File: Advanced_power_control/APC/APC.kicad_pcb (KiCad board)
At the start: 4 copper layers, 60.2 x 84.5 mm, 51 parts, among them J1 AVR-JTAG-10, J10 CMD_IN, J11 PWR_V_SEL, J12 12/24 V_IN, J13 220 OUT, J2 EM_STOP_INT, J3 STATUS_LED, J4 EM_STOP, J5 PWR_BTN, J6 POWER_LED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

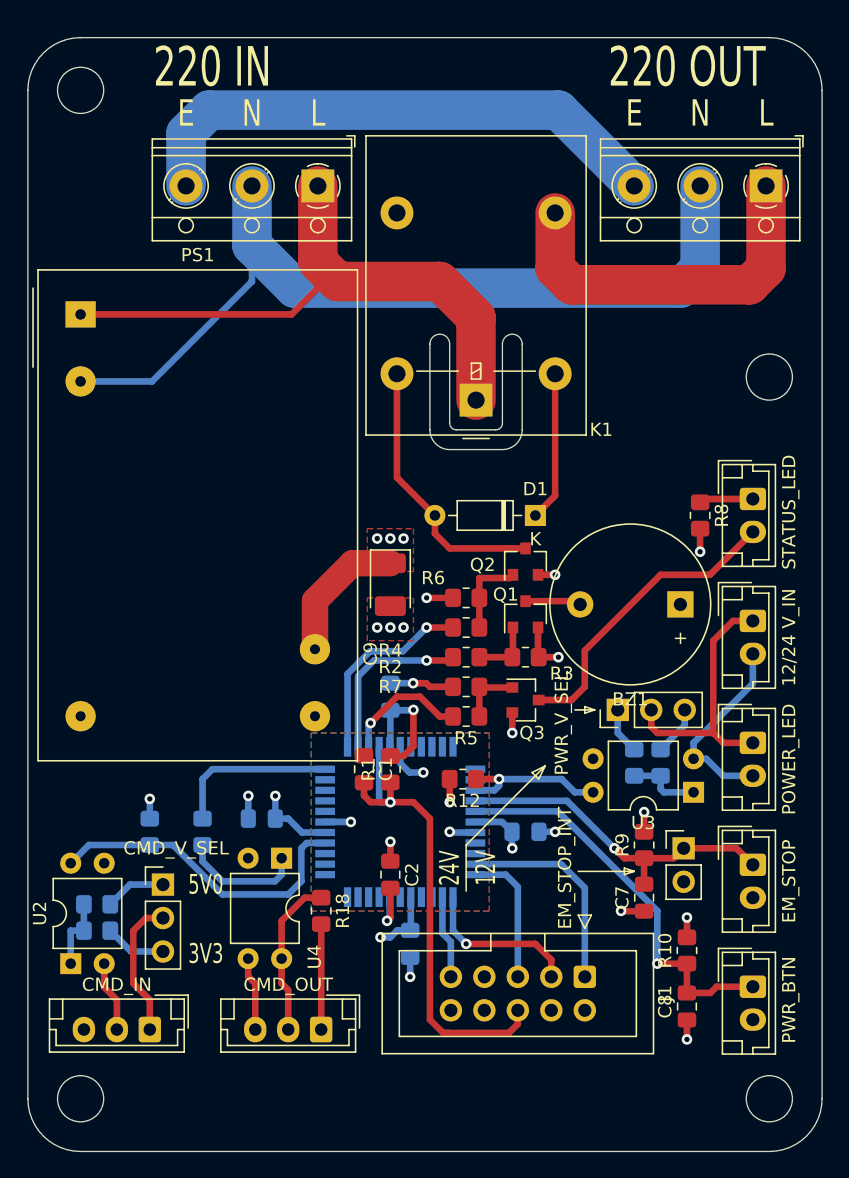
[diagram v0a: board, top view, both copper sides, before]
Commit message: minimize pcb size
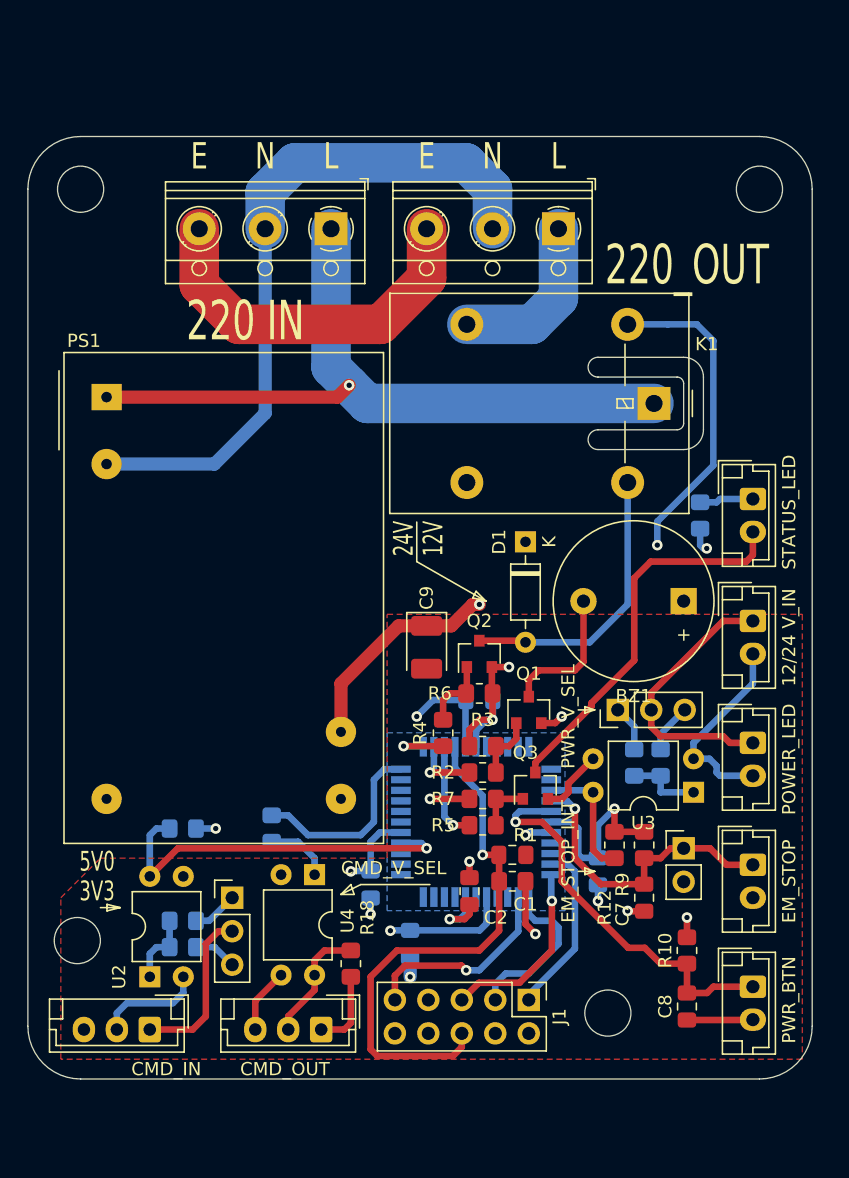
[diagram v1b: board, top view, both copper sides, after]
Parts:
- J1: footprint Connector_IDC:IDC-Header_2x05_P2.54mm_Vertical -> Connector_PinHeader_2.54mm:PinHeader_2x05_P2.54mm_Vertical
- J13: value 220 OUT -> 220_OUT
- R8: moved to B.Cu
- moved J13 16.1 mm to (126.5, 37.0)
- moved K1 13.5 mm to (133.8, 50.2), turned to 270 degrees
- moved C1 13.0 mm to (123.0, 84.5), turned to 180 degrees
- moved R1 12.6 mm to (123.0, 86.5), turned to 0 degrees
- moved R12 12.5 mm to (130.8, 83.8), turned to 90 degrees
- moved C5 9.65 mm to (112.2, 86.8), turned to 90 degrees
- moved R2 8.84 mm to (120.8, 78.2)
- moved R7 8.59 mm to (120.8, 80.2)
- moved R5 8.34 mm to (120.8, 82.2)
- moved R4 8.19 mm to (117.8, 75.2), turned to 270 degrees
- moved Q2 7.83 mm to (120.5, 69.2)
- moved R3 7.49 mm to (120.8, 76.2), turned to 0 degrees
- moved R6 7.32 mm to (120.5, 72.2), turned to 180 degrees
- moved Q1 7.25 mm to (124.2, 73.5)
- moved C3 6.75 mm to (120.5, 72.8), turned to 180 degrees
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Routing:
- net +5V: track 197.9 -> 87.8 mm, vias 12 -> 10
- net /N: track 70.1 -> 52.4 mm
- net /L_O: track 27.5 -> 13.0 mm
- net /E: track 41.1 -> 27.9 mm
- net /PWR: track 15.0 -> 5.02 mm
- net /TDI: track 6.32 -> 15.5 mm, vias 0 -> 1
- net /S_STATE: track 13.1 -> 5.07 mm
- net GND: track 29.8 -> 36.3 mm, vias 17 -> 10
- net Net-(BZ1-Pad2): track 4.25 -> 10.6 mm
- net Net-(J3-Pad2): track 23.1 -> 29.3 mm
- net /CMD_IN: track 24.5 -> 29.0 mm, vias 0 -> 1
- net /RST: track 36.8 -> 41.2 mm
- net Net-(R13-Pad1): track 9.33 -> 5.02 mm
- net /TMS: track 10.4 -> 14.2 mm, vias 0 -> 1
- net /S: track 12.2 -> 9.14 mm
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- added copper zone on In2.Cu, net +5V
- removed copper zone on F.Cu, net +5V
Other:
- board size 60.2 x 84.5 mm -> 59.5 x 71.5 mm

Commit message: Update APC.kicad_pcb
PreFinal correction
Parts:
- J12: value 12/24 V_IN -> 12/24V
- J6: value POWER_LED -> PWR_LED
- moved D1 9.25 mm to (114.8, 60.5), turned to 0 degrees
- moved R13 4.03 mm to (108.8, 83.0), turned to 0 degrees
- moved BZ1 2.75 mm to (133.2, 65.2)
- moved R18 2.70 mm to (112.2, 90.5)
- moved J9 2.47 mm to (103.5, 86.0)
- moved U2 2.24 mm to (97.5, 92.8)
- moved C3 2.14 mm to (118.5, 72.0), turned to 0 degrees
- moved R14 2.02 mm to (99.8, 90.5)
- moved R15 2.02 mm to (99.8, 88.5)
- moved U4 1.68 mm to (109.5, 85.2)
- moved J10 1.50 mm to (97.0, 97.8)
- moved J7 1.50 mm to (110.8, 37.0)
- moved J13 1.00 mm to (127.5, 37.0)
- renumbered J1 to JTAG
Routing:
- net GND: track 36.3 -> 0.00 mm, vias 10 -> 67
- net +5V: track 87.8 -> 96.9 mm
- net /CMD_OUT: track 14.4 -> 8.75 mm
- net /CMD_IN: track 29.0 -> 24.8 mm
- net /S: track 9.14 -> 13.2 mm
- net /E: track 27.9 -> 25.0 mm
- net /V: track 5.96 -> 8.83 mm
- net Net-(BZ1-Pad2): track 10.6 -> 7.83 mm
- net Net-(J3-Pad2): track 29.3 -> 31.8 mm
- net /G: track 4.94 -> 7.19 mm
- net /P_ON: track 21.7 -> 19.7 mm
- net Net-(R13-Pad1): track 5.02 -> 2.97 mm
- net /V_SEL: track 20.8 -> 22.5 mm
- net Net-(J10-Pad2): track 8.14 -> 9.34 mm
- net /CMD_V_IN: track 12.6 -> 13.5 mm
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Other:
- board size 59.5 x 71.5 mm -> 55.8 x 70.5 mm

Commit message: Release 1.0
Update pcb
Add assembly pdf-files
Add gerber files
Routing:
- net (no net): track 0.00 -> 22.0 mm
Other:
- board text added: "Advanced Power V1.0 Controller"

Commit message: some changes
Change vias size fo jlcpcb
Add gerbers in zip archive
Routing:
- net +5V: track 96.9 -> 97.6 mm
- net GND: vias 67 -> 66
